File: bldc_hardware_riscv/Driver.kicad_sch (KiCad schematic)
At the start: 95 parts

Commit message: add debug RX/TX, fix CH9141K footprint error, add 12V detection
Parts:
- added U (x2): (no value), symbol Device:R
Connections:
- net 12V: now also U.1
- net GND: now also U.2
- new net ADC_V12V: U.1, U.2
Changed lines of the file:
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@@
   (junction (at 106.68 147.32) (diameter 0) (color 0 0 0 0)
   )
+  (junction (at 265.43 127) (diameter 0) (color 0 0 0 0)
+  )
   (junction (at 48.26 133.35) (diameter 0) (color 0 0 0 0)
   )
@@
     (stroke (width 0) (type default))
   )
+  (wire (pts (xy 276.86 127) (xy 276.86 129.54))
+    (stroke (width 0) (type default))
+  )
   (wire (pts (xy 219.71 41.275) (xy 219.71 43.18))
     (stroke (width 0) (type default))
@@
     (stroke (width 0) (type default))
   )
+  (wire (pts (xy 275.59 127) (xy 276.86 127))
+    (stroke (width 0) (type default))
+  )
   (wire (pts (xy 232.41 80.01) (xy 232.41 82.55))
     (stroke (width 0) (type default))
@@
     (stroke (width 0) (type default))
   )
+  (wire (pts (xy 250.19 127) (xy 255.27 127))
+    (stroke (width 0) (type default))
+  )
   (wire (pts (xy 74.93 53.34) (xy 118.11 53.34))
     (stroke (width 0) (type default))
@@
     (stroke (width 0) (type default))
   )
+  (wire (pts (xy 265.43 121.92) (xy 265.43 127))
+    (stroke (width 0) (type default))
+  )
   (wire (pts (xy 232.41 75.565) (xy 233.68 75.565))
     (stroke (width 0) (type default))
@@
     (stroke (width 0) (type default))
   )
+  (wire (pts (xy 265.43 127) (xy 267.97 127))
+    (stroke (width 0) (type default))
+  )
   (wire (pts (xy 81.28 182.88) (xy 85.09 182.88))
     (stroke (width 0) (type default))
@@
     (stroke (width 0) (type default))
   )
+  (wire (pts (xy 266.7 121.92) (xy 265.43 121.92))
+    (stroke (width 0) (type default))
+  )
   (wire (pts (xy 262.89 114.3) (xy 261.62 114.3))
     (stroke (width 0) (type default))
@@
   )
   (wire (pts (xy 26.67 162.56) (xy 33.02 162.56))
+    (stroke (width 0) (type default))
+  )
+  (wire (pts (xy 262.89 127) (xy 265.43 127))
     (stroke (width 0) (type default))
   )
@@
     (effects (font (size 1.27 1.27)) (justify left bottom))
   )
+  (label "12V" (at 250.19 127 0) (fields_autoplaced)
+    (effects (font (size 1.27 1.27)) (justify left bottom))
+  )
   (label "LO3" (at 76.2 55.88 0) (fields_autoplaced)
     (effects (font (size 1.27 1.27)) (justify left bottom))
@@
   (hierarchical_label "HIN3" (shape input) (at 49.53 33.02 180) (fields_autoplaced)
     (effects (font (size 1.27 1.27)) (justify right))
+  )
+  (hierarchical_label "ADC_V12V" (shape output) (at 266.7 121.92 0) (fields_autoplaced)
+    (effects (font (size 1.27 1.27)) (justify left))
   )
   (hierarchical_label "ADC_Vin" (shape output) (at 266.7 149.86 0) (fields_autoplaced)
@@
     )
     (property "Value" "" (id 1) (at 125.73 167.64 90)
-      (effects (font (size 1.27 1.27)))
+      (effects (font (size 1.016 1.016)))
     )
     (property "Footprint" "" (id 2) (at 125.73 169.418 90)
@@
     (pin "2")
   )
+  (symbol (lib_id "Device:R") (at 271.78 127 90) (unit 1)
+    (in_bom yes) (on_board yes)
+    (default_instance (reference "U") (unit 1) (value "") (footprint ""))
+    (property "Reference" "U" (id 0) (at 270.51 129.54 90)
+      (effects (font (size 1.27 1.27)) (justify right))
+    )
+    (property "Value" "" (id 1) (at 271.78 127 90)
+      (effects (font (size 1.27 1.27)))
+    )
+    (property "Footprint" "" (id 2) (at 271.78 128.778 90)
+      (effects (font (size 1.27 1.27)) hide)
+    )
+    (property "Datasheet" "~" (id 3) (at 271.78 127 0)
+      (effects (font (size 1.27 1.27)) hide)
+    )
+    (pin "1")
+    (pin "2")
+  )
   (symbol (lib_id "Diode:1N4448W") (at 104.14 17.78 180) (unit 1)
     (in_bom yes) (on_board yes)
@@
     )
     (property "Datasheet" "" (id 3) (at 246.38 157.48 0)
+      (effects (font (size 1.27 1.27)) hide)
+    )
+    (pin "1")
+  )
+  (symbol (lib_id "power:GND") (at 276.86 129.54 0) (unit 1)
+    (in_bom yes) (on_board yes)
+    (default_instance (reference "U") (unit 1) (value "") (footprint ""))
+    (property "Reference" "U" (id 0) (at 276.86 135.89 0)
+      (effects (font (size 1.27 1.27)) hide)
+    )
+    (property "Value" "" (id 1) (at 276.86 133.35 0)
+      (effects (font (size 1.27 1.27)))
+    )
+    (property "Footprint" "" (id 2) (at 276.86 129.54 0)
+      (effects (font (size 1.27 1.27)) hide)
+    )
+    (property "Datasheet" "" (id 3) (at 276.86 129.54 0)
       (effects (font (size 1.27 1.27)) hide)
     )
@@
       (effects (font (size 1.27 1.27)) hide)
     )
+    (pin "1")
+    (pin "2")
+  )
+  (symbol (lib_id "Device:R") (at 259.08 127 90) (unit 1)
+    (in_bom yes) (on_board yes)
+    (default_instance (reference "U") (unit 1) (value "") (footprint ""))
+    (property "Reference" "U" (id 0) (at 257.81 129.54 90)
+      (effects (font (size 1.27 1.27)) (justify right))
+    )
+    (property "Value" "" (id 1) (at 259.08 127 90)
+      (effects (font (size 1.016 1.016)))
+    )
+    (property "Footprint" "" (id 2) (at 259.08 128.778 90)
+      (effects (font (size 1.27 1.27)) hide)
+    )
+    (property "Datasheet" "~" (id 3) (at 259.08 127 0)
+      (effects (font (size 1.27 1.27)) hide)
+    )

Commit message: use hall current sensor (60A limit), use keystone terminal, support up to 120V input
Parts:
- removed U (x5): (no value), symbol BLDC_Library:CON-T
- removed U (x6): (no value), symbol Device:C
- removed U (x3): (no value), symbol BLDC_Library:MAX9919
- removed U (x12): (no value), symbol Device:R
- added D: D_Zener, symbol Device:D_Zener
- added Q: 2SD1047, Package_TO_SOT_THT:TO-3PB-3_Vertical, symbol Transistor_BJT:2SD1047
- added U (x3): MT9222WT-65BR5, Package_SO:SOIC-16W_7.5x10.3mm_P1.27mm, symbol BLDC_Library:MT9222WT-65BR5
- added U (x12): (no value), symbol Device:C
- added U (x7): (no value), symbol Device:R
- added U (x5): (no value), symbol BLDC_Library:CON-T
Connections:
- net 5V: now also U.10 (VCC), U.10 (VCC), U.10 (VCC), U.2, U.2, U.2, U.2, U.2, U.2
- net ADC_CS1: now also U.1, U.1, U.2
- net ADC_CS2: now also U.1, U.1, U.2
- net ADC_CS3: now also U.1, U.1, U.2
- net GND: now also D.2 (A), U.1, U.1, U.1, U.1, U.1, U.1, U.1, U.15 (GND), U.15 (GND), U.15 (GND), U.2, U.2, U.2, U.2, U.2, U.2, U.2, U.2, U.2
- net PhaseA: now also U.1, U.5 (IP-), U.6 (IP-), U.7 (IP-), U.8 (IP-)
- net PhaseB: now also U.1, U.5 (IP-), U.6 (IP-), U.7 (IP-), U.8 (IP-)
- net PhaseC: now also U.1, U.5 (IP-), U.6 (IP-), U.7 (IP-), U.8 (IP-)
- net VS1: now also U.1 (IP+), U.2 (IP+), U.3 (IP+), U.4 (IP+)
- net VS2: now also U.1 (IP+), U.2 (IP+), U.3 (IP+), U.4 (IP+)
- net VS3: now also U.1 (IP+), U.2 (IP+), U.3 (IP+), U.4 (IP+)
- net 72V renamed 99V
- net 99V: now also Q.2 (C), U.1, U.2; no longer U.1, U.1, U.1, U.4 (VIN)
- new net: U.1, U.12 (OUT) (x3)
- new net: U.1, U.13 (FLT) (x3)
- new net: D.1 (K), Q.1 (B), U.1
- new net 75V: Q.3 (E), U.1, U.1, U.1, U.4 (VIN)
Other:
- note added: "1.1.0"
- note added: "Max input: 80V"
- note removed: "1.0.1"
- moved on the sheet: U

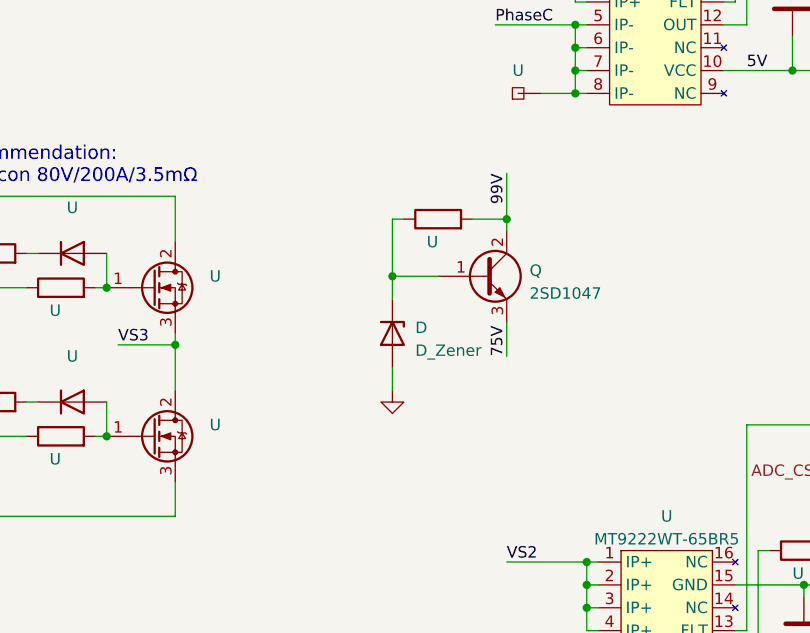
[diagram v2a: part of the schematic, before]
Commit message: add missed caps
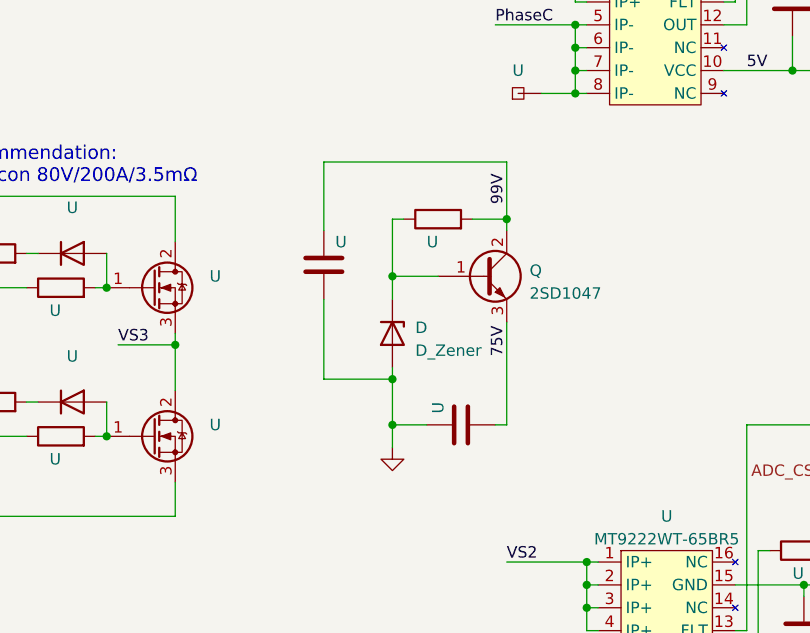
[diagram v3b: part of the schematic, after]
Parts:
- added U (x2): (no value), symbol Device:C
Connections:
- net 75V: now also U.2
- net 99V: now also U.1
- net GND: now also U.1, U.2
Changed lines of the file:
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@@
   (junction (at 21.59 97.79) (diameter 0) (color 0 0 0 0)
   )
+  (junction (at 167.64 97.79) (diameter 0) (color 0 0 0 0)
+  )
   (junction (at 93.98 107.95) (diameter 0) (color 0 0 0 0)
   )
@@
   (junction (at 99.06 135.89) (diameter 0) (color 0 0 0 0)
   )
+  (junction (at 167.64 92.71) (diameter 0) (color 0 0 0 0)
+  )
   (junction (at 105.41 33.02) (diameter 0) (color 0 0 0 0)
   )
@@
     (stroke (width 0) (type default))
   )
-  (wire (pts (xy 167.64 91.44) (xy 167.64 93.98))
+  (wire (pts (xy 167.64 91.44) (xy 167.64 92.71))
     (stroke (width 0) (type default))
   )
@@
     (stroke (width 0) (type default))
   )
+  (wire (pts (xy 160.02 83.82) (xy 160.02 92.71))
+    (stroke (width 0) (type default))
+  )
   (wire (pts (xy 167.64 74.93) (xy 167.64 81.28))
     (stroke (width 0) (type default))
@@
     (stroke (width 0) (type default))
   )
-  (wire (pts (xy 180.34 69.85) (xy 180.34 74.93))
+  (wire (pts (xy 180.34 68.58) (xy 180.34 74.93))
     (stroke (width 0) (type default))
   )
@@
     (stroke (width 0) (type default))
   )
+  (wire (pts (xy 179.07 97.79) (xy 180.34 97.79))
+    (stroke (width 0) (type default))
+  )
   (wire (pts (xy 264.16 63.5) (xy 262.89 63.5))
     (stroke (width 0) (type default))
@@
     (stroke (width 0) (type default))
   )
+  (wire (pts (xy 160.02 76.2) (xy 160.02 68.58))
+    (stroke (width 0) (type default))
+  )
   (wire (pts (xy 46.99 55.88) (xy 52.07 55.88))
     (stroke (width 0) (type default))
@@
     (stroke (width 0) (type default))
   )
+  (wire (pts (xy 167.64 97.79) (xy 171.45 97.79))
+    (stroke (width 0) (type default))
+  )
   (wire (pts (xy 161.29 135.89) (xy 157.48 135.89))
     (stroke (width 0) (type default))
@@
     (stroke (width 0) (type default))
   )
+  (wire (pts (xy 160.02 92.71) (xy 167.64 92.71))
+    (stroke (width 0) (type default))
+  )
   (wire (pts (xy 234.95 76.2) (xy 233.68 76.2))
     (stroke (width 0) (type default))
@@
     (stroke (width 0) (type default))
   )
+  (wire (pts (xy 160.02 68.58) (xy 180.34 68.58))
+    (stroke (width 0) (type default))
+  )
   (wire (pts (xy 62.23 133.35) (xy 62.23 123.19))
     (stroke (width 0) (type default))
@@
     (stroke (width 0) (type default))
   )
-  (wire (pts (xy 180.34 86.36) (xy 180.34 90.17))
+  (wire (pts (xy 180.34 86.36) (xy 180.34 97.79))
     (stroke (width 0) (type default))
   )
@@
     (stroke (width 0) (type default))
   )
+  (wire (pts (xy 167.64 97.79) (xy 167.64 100.33))
+    (stroke (width 0) (type default))
+  )
   (wire (pts (xy 219.71 105.41) (xy 218.44 105.41))
     (stroke (width 0) (type default))
@@
     (stroke (width 0) (type default))
   )
+  (wire (pts (xy 167.64 92.71) (xy 167.64 97.79))
+    (stroke (width 0) (type default))
+  )
   (wire (pts (xy 76.2 35.56) (xy 74.93 35.56))
     (stroke (width 0) (type default))
@@
     (effects (font (size 1.27 1.27)) (justify right))
   )
+  (symbol (lib_id "Device:C") (at 160.02 80.01 0) (unit 1)
+    (in_bom yes) (on_board yes)
+    (default_instance (reference "U") (unit 1) (value "") (footprint ""))
+    (property "Reference" "U" (id 0) (at 161.29 77.47 0)
+      (effects (font (size 1.27 1.27)) (justify left))
+    )
+    (property "Value" "" (id 1) (at 161.29 82.55 0)
+      (effects (font (size 1.27 1.27)) (justify left))
+    )
+    (property "Footprint" "" (id 2) (at 160.9852 83.82 0)
+      (effects (font (size 1.27 1.27)) hide)
+    )
+    (property "Datasheet" "~" (id 3) (at 160.02 80.01 0)
+      (effects (font (size 1.27 1.27)) hide)
+    )
+    (pin "1")
+    (pin "2")
+  )
   (symbol (lib_id "power:GND") (at 227.33 46.99 0) (unit 1)
     (in_bom yes) (on_board yes)
@@
     (pin "1")
   )
+  (symbol (lib_id "Device:C") (at 175.26 97.79 90) (unit 1)
+    (in_bom yes) (on_board yes)
+    (default_instance (reference "U") (unit 1) (value "") (footprint ""))
+    (property "Reference" "U" (id 0) (at 172.72 96.52 0)
+      (effects (font (size 1.27 1.27)) (justify left))
+    )
+    (property "Value" "" (id 1) (at 177.8 96.52 0)
+      (effects (font (size 1.27 1.27)) (justify left))
+    )
+    (property "Footprint" "" (id 2) (at 179.07 96.8248 0)
+      (effects (font (size 1.27 1.27)) hide)
+    )
+    (property "Datasheet" "~" (id 3) (at 175.26 97.79 0)
+      (effects (font (size 1.27 1.27)) hide)
+    )
+    (pin "1")
+    (pin "2")
+  )
   (symbol (lib_id "power:GND") (at 22.86 111.76 0) (unit 1)
     (in_bom yes) (on_board yes)
@@
     (pin "2")
   )
-  (symbol (lib_id "power:GND") (at 167.64 93.98 0) (unit 1)
+  (symbol (lib_id "power:GND") (at 167.64 100.33 0) (unit 1)
     (in_bom yes) (on_board yes)
     (default_instance (reference "U") (unit 1) (value "") (footprint ""))
-    (property "Reference" "U" (id 0) (at 167.64 100.33 0)
+    (property "Reference" "U" (id 0) (at 167.64 106.68 0)
       (effects (font (size 1.27 1.27)) hide)
     )
-    (property "Value" "" (id 1) (at 167.64 97.79 0)
+    (property "Value" "" (id 1) (at 167.64 104.14 0)
       (effects (font (size 1.27 1.27)))
     )
-    (property "Footprint" "" (id 2) (at 167.64 93.98 0)
+    (property "Footprint" "" (id 2) (at 167.64 100.33 0)
       (effects (font (size 1.27 1.27)) hide)
     )
-    (property "Datasheet" "" (id 3) (at 167.64 93.98 0)
+    (property "Datasheet" "" (id 3) (at 167.64 100.33 0)
       (effects (font (size 1.27 1.27)) hide)
     )
